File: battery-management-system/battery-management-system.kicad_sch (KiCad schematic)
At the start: 4 parts

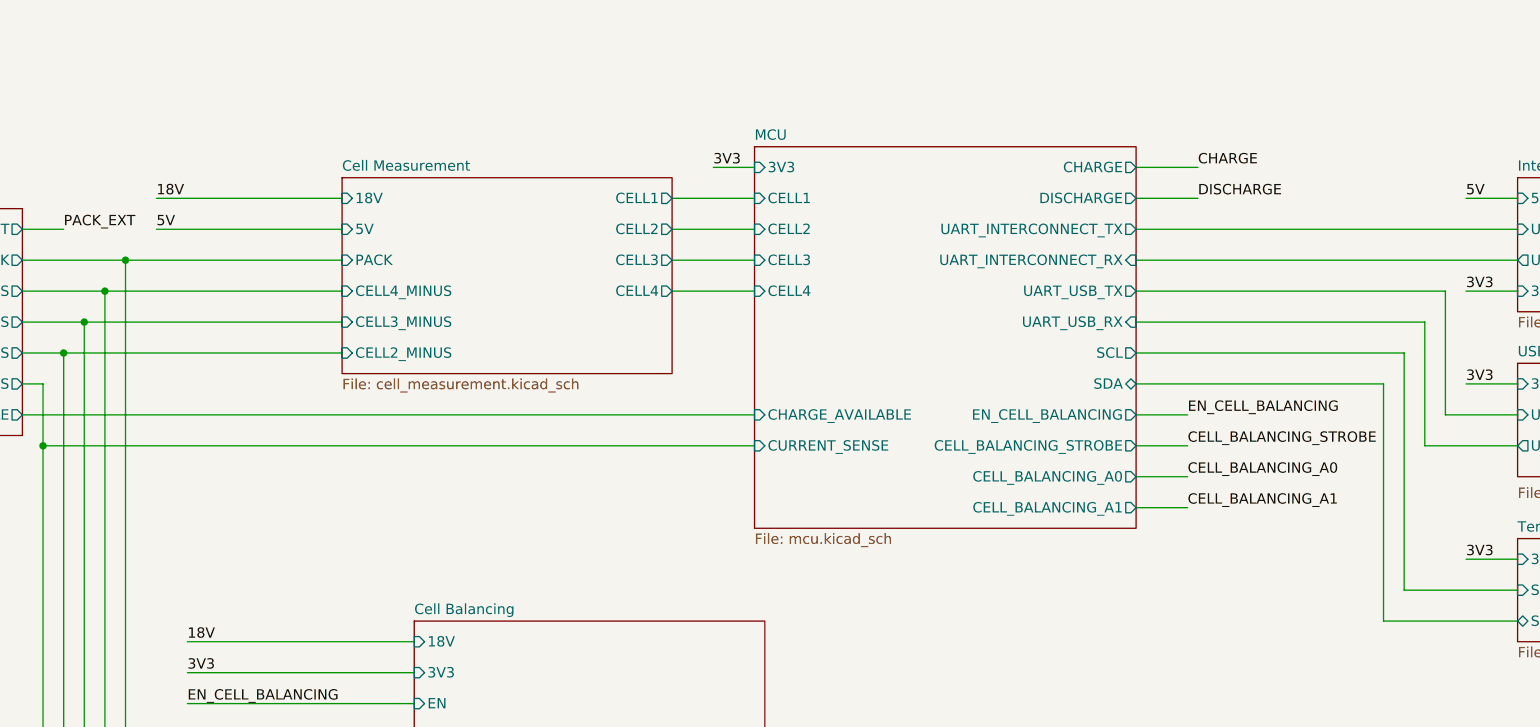
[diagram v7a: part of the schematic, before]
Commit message: add enable input for cell measurement
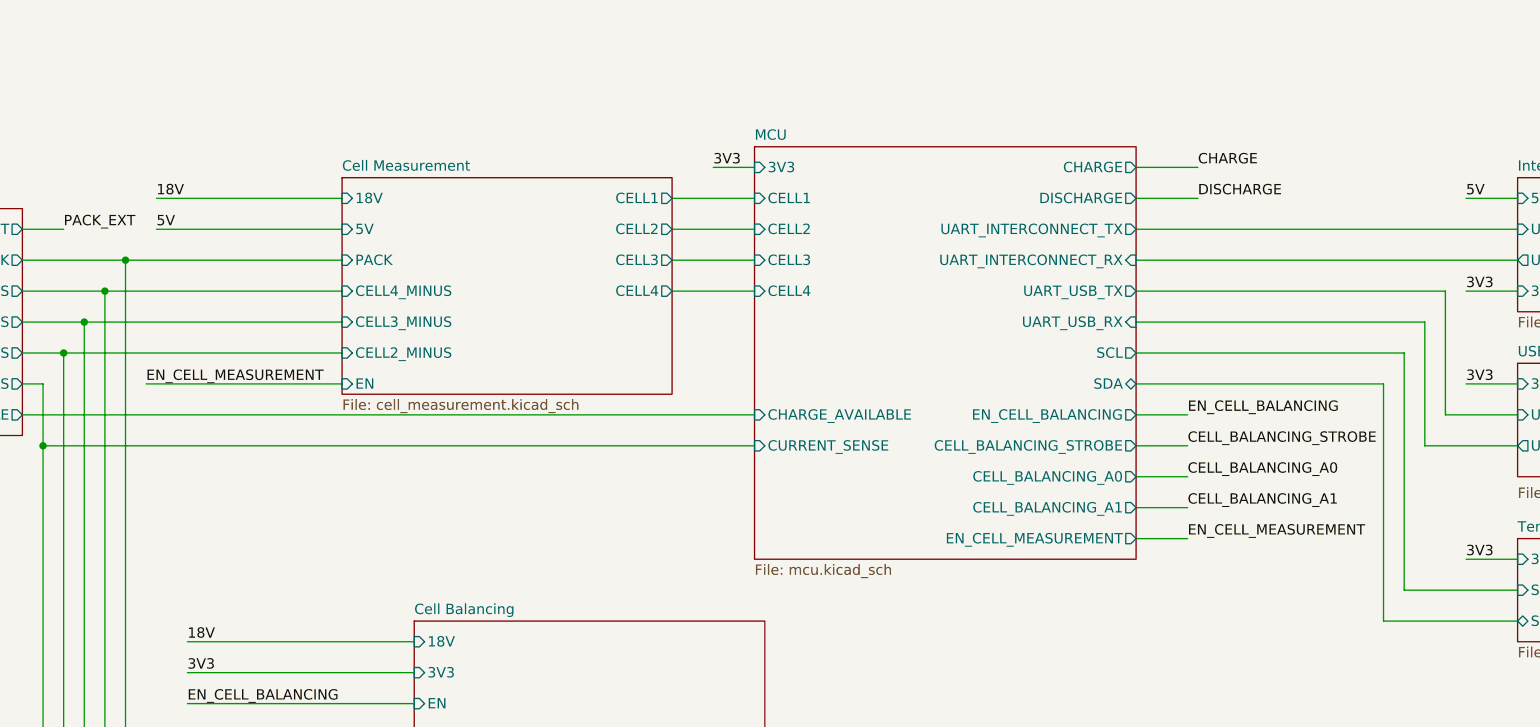
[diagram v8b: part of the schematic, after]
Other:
- sheet Cell Measurement ports: added EN; removed none
- sheet MCU ports: added EN_CELL_MEASUREMENT; removed none
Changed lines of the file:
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@@
+    (stroke (width 0) (type default))
+  )
+  (wire (pts (xy 97.79 102.87) (xy 73.66 102.87))
     (stroke (width 0) (type default))
   )
@@
     (stroke (width 0) (type default))
   )
+  (wire (pts (xy 195.58 121.92) (xy 201.93 121.92))
+    (stroke (width 0) (type default))
+  )
   (wire (pts (xy 195.58 102.87) (xy 226.06 102.87))
     (stroke (width 0) (type default))
@@
     (effects (font (size 1.27 1.27)) (justify left bottom))
   )
+  (label "EN_CELL_MEASUREMENT" (at 73.66 102.87 0) (fields_autoplaced)
+    (effects (font (size 1.27 1.27)) (justify left bottom))
+  )
   (label "5V" (at 236.22 80.01 0) (fields_autoplaced)
     (effects (font (size 1.27 1.27)) (justify left bottom))
@@
   )
   (label "3V3" (at 78.74 138.43 0) (fields_autoplaced)
+    (effects (font (size 1.27 1.27)) (justify left bottom))
+  )
+  (label "EN_CELL_MEASUREMENT" (at 201.93 121.92 0) (fields_autoplaced)
     (effects (font (size 1.27 1.27)) (justify left bottom))
   )
@@
   (symbol (lib_id "power:GND") (at 259.08 41.91 0) (unit 1)
     (in_bom yes) (on_board yes) (dnp no) (fields_autoplaced)
-    (property "Reference" "#PWR011" (at 259.08 48.26 0)
+    (property "Reference" "#PWR04" (at 259.08 48.26 0)
       (effects (font (size 1.27 1.27)) hide)
     )
@@
       (project "battery-management-system"
         (path "/5272f0ff-3069-41a9-bca2-80beede8b4b2"
-          (reference "#PWR011") (unit 1)
+          (reference "#PWR04") (unit 1)
         )
       )
@@
     )
   )
-  (sheet (at 97.79 77.47) (size 40.64 24.13) (fields_autoplaced)
+  (sheet (at 97.79 77.47) (size 40.64 26.67) (fields_autoplaced)
     (stroke (width 0.1524) (type solid))
     (fill (color 0 0 0 0.0000))
@@
       (effects (font (size 1.27 1.27)) (justify left bottom))
     )
-    (property "Sheetfile" "cell_measurement.kicad_sch" (at 97.79 102.1846 0)
+    (property "Sheetfile" "cell_measurement.kicad_sch" (at 97.79 104.7246 0)
       (effects (font (size 1.27 1.27)) (justify left top))
     )
@@
     )
     (pin "18V" input (at 97.79 80.01 180)
+      (effects (font (size 1.27 1.27)) (justify left))
+    )
+    (pin "EN" input (at 97.79 102.87 180)
       (effects (font (size 1.27 1.27)) (justify left))
     )
@@
     )
   )
-  (sheet (at 148.59 73.66) (size 46.99 46.99) (fields_autoplaced)
+  (sheet (at 148.59 73.66) (size 46.99 50.8) (fields_autoplaced)
     (stroke (width 0.1524) (type solid))
     (fill (color 0 0 0 0.0000))
@@
       (effects (font (size 1.27 1.27)) (justify left bottom))
     )
-    (property "Sheetfile" "mcu.kicad_sch" (at 148.59 121.2346 0)
+    (property "Sheetfile" "mcu.kicad_sch" (at 148.59 125.0446 0)
       (effects (font (size 1.27 1.27)) (justify left top))
     )
@@
       (effects (font (size 1.27 1.27)) (justify right))
     )
+    (pin "EN_CELL_MEASUREMENT" output (at 195.58 121.92 0)
+      (effects (font (size 1.27 1.27)) (justify right))
+    )
